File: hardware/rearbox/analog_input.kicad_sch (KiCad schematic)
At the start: 14 parts, among them U27 MCP6N11T-002, U28 MCP6001

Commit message: Changed power section
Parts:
- renumbered C66 to C36, C67 to C37, C68 to C38, C69 to C39, R120 to R73, R121 to R74, R122 to R75, R123 to R76, TP56 to TP24, TP57 to TP25, TP58 to TP26, TP59 to TP27, U27 to U13, U28 to U14

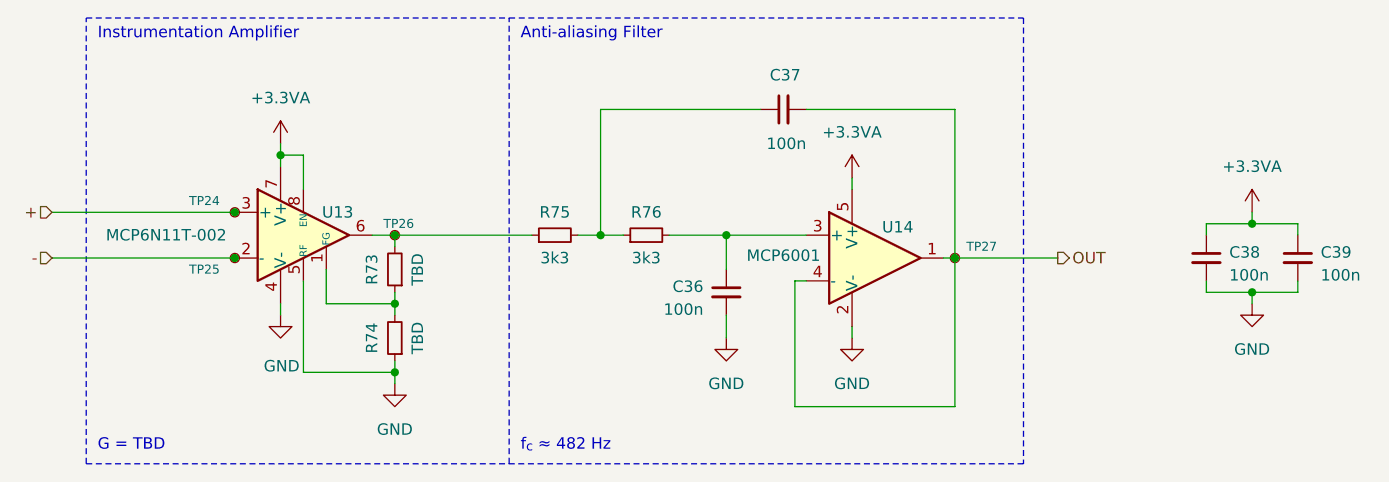
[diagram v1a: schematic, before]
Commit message: Deleted measurement systems for new iteration
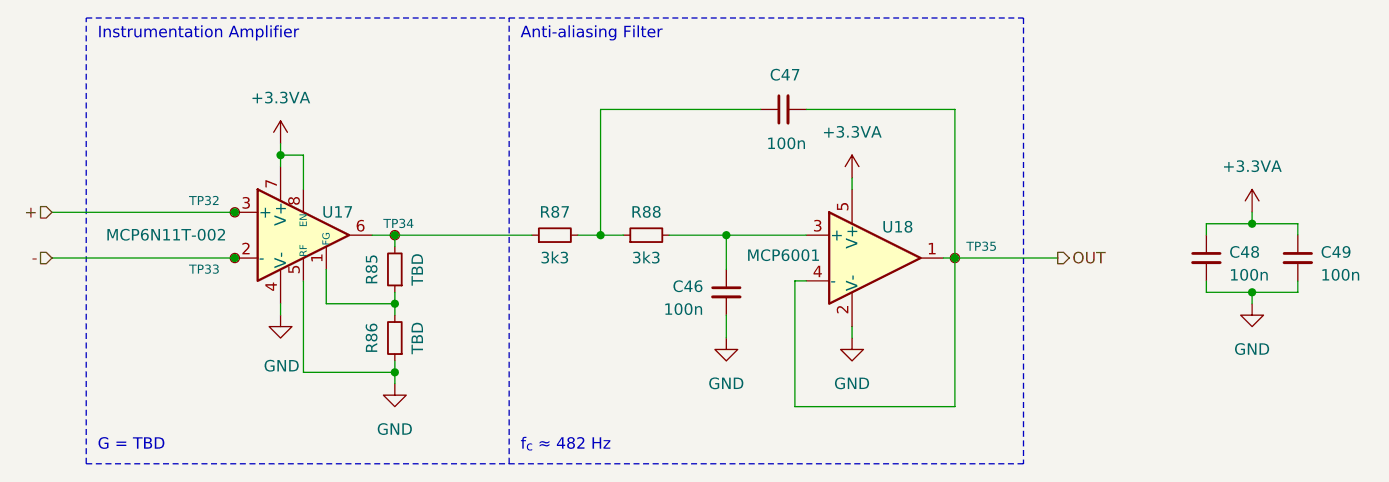
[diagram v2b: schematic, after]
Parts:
- renumbered C36 to C46, C37 to C47, C38 to C48, C39 to C49, R73 to R85, R74 to R86, R75 to R87, R76 to R88, TP24 to TP32, TP25 to TP33, TP26 to TP34, TP27 to TP35, U13 to U17, U14 to U18
